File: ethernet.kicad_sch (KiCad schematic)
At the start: 65 parts, among them Q5001 DMG1012T, Q5002 DMG1012T, U1002 AM6231ASGGGAALW, U5001 HR911130A, U5002 RTL8211F-CG, U5003 TPD4E05U06DQA, U5004 TPD4E05U06DQA

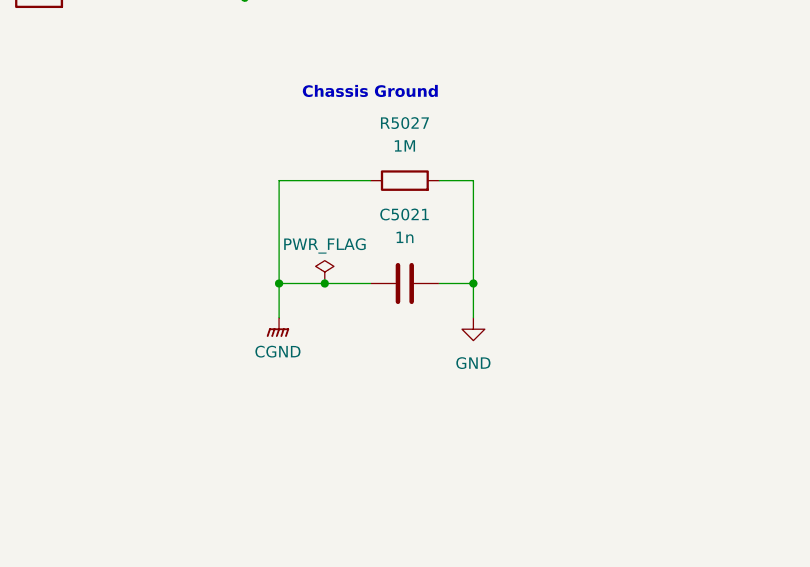
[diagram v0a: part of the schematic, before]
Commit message: All capacitors and crystals added to BOM. 150u cap for USB A changed to tantalum and rerouted
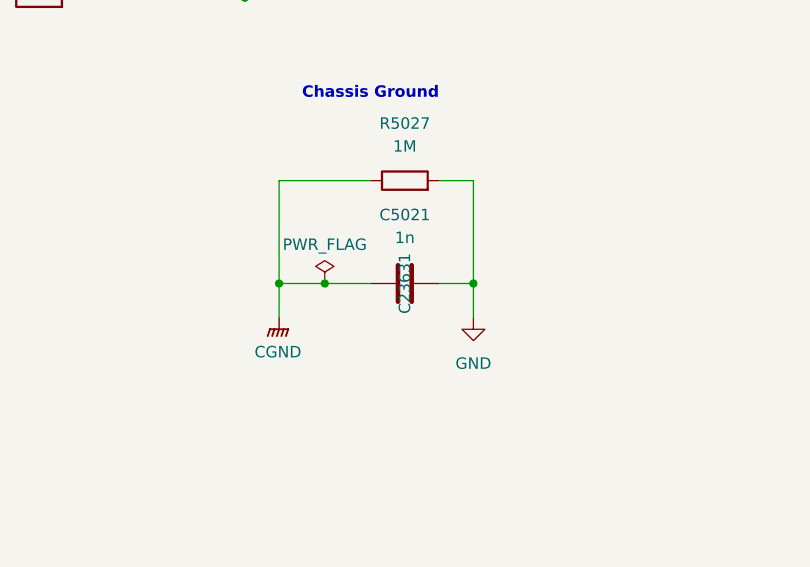
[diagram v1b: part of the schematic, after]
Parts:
- C5021: JLCPCB Part# (none) -> C23631
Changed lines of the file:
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@@
 			)
 		)
-		(property "JLCPCB Part#" ""
+		(property "JLCPCB Part#" " C23631"
 			(at 427.99 307.34 0)
 			(effects

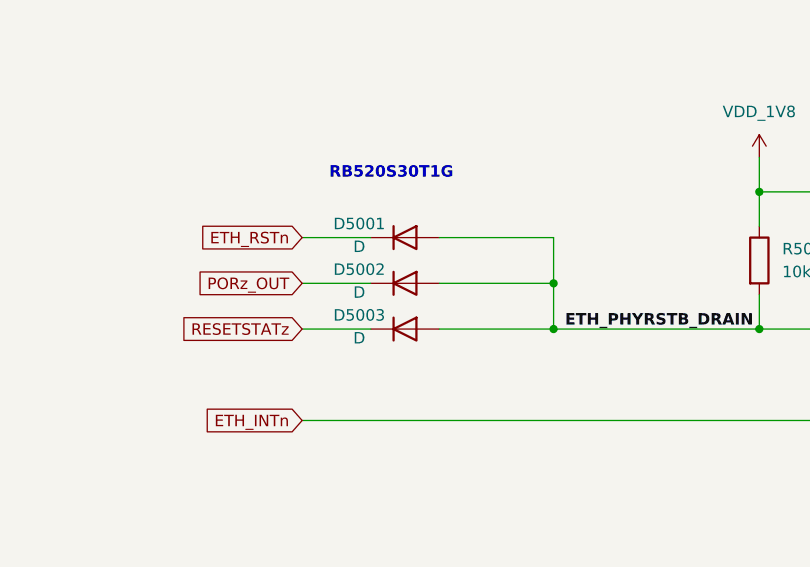
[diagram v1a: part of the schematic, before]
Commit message: Added diode and tvs diode JLC part numbers to BOM. Also fixed tvs diode footprint
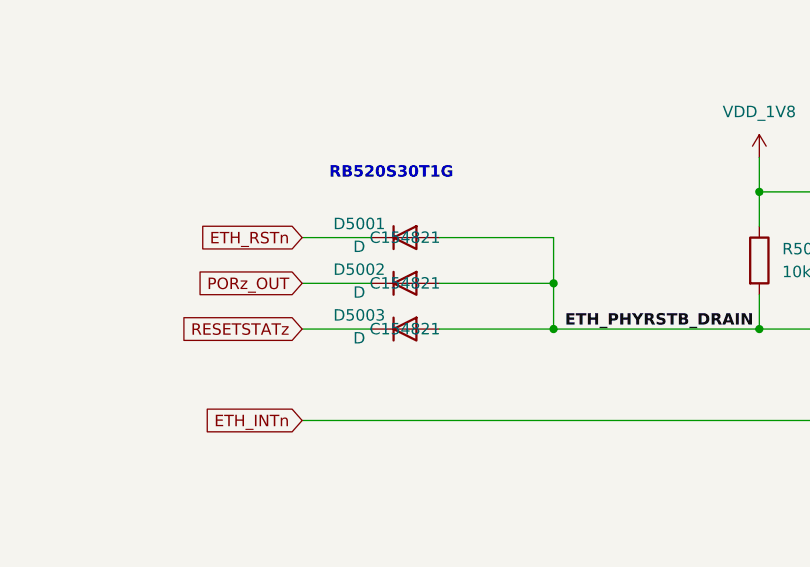
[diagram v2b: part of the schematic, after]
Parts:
- D5001, D5002, D5003: JLCPCB Part# (none) -> C154821
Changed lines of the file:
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@@
 			)
 		)
-		(property "JLCPCB Part#" ""
+		(property "JLCPCB Part#" "C154821"
 			(at 148.59 339.09 0)
 			(effects
@@
 			)
 		)
-		(property "JLCPCB Part#" ""
+		(property "JLCPCB Part#" "C154821"
 			(at 148.59 328.93 0)
 			(effects
@@
 			)
 		)
-		(property "JLCPCB Part#" ""
+		(property "JLCPCB Part#" "C154821"
 			(at 148.59 334.01 0)
 			(effects

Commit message: All JLC part numbers added to BOM except LEDs
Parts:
- FB5001, FB5002: JLCPCB Part# (none) -> C76891
- L5001: JLCPCB Part# (none) -> C391305
- Q5001, Q5002: JLCPCB Part# (none) -> C20512
- R5001, R5002, R5003, R5020, R5022, R5024: JLCPCB Part# (none) -> C105871
- R5004: JLCPCB Part# (none) -> C114759
- R5005, R5006, R5007: JLCPCB Part# (none) -> C106235
- R5008, R5009, R5010, R5011, R5012, R5013, R5014, R5015, R5016, R5017, R5018, R5019, R5021: JLCPCB Part# (none) -> C114765
- R5023: JLCPCB Part# (none) -> C145071
- R5025, R5026: JLCPCB Part# (none) -> C276273
- R5027: JLCPCB Part# (none) -> C108083
- R5028, R5029, R5030, R5031: JLCPCB Part# (none) -> C60490
- U1002: JLCPCB Part# (none) -> C7072556
- U5001: JLCPCB Part# (none) -> C54408
- U5002: JLCPCB Part# (none) -> C187932
- U5003, U5004: JLCPCB Part# (none) -> C138714
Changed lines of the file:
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@@
 			)
 		)
-		(property "JLCPCB Part#" ""
+		(property "JLCPCB Part#" "C76891"
 			(at 214.63 130.81 0)
 			(effects
@@
 			)
 		)
-		(property "JLCPCB Part#" ""
+		(property "JLCPCB Part#" " C276273"
 			(at 387.35 265.43 0)
 			(effects
@@
 			)
 		)
-		(property "JLCPCB Part#" ""
+		(property "JLCPCB Part#" "C114765"
 			(at 240.03 182.88 0)
 			(effects
@@
 			)
 		)
-		(property "JLCPCB Part#" ""
+		(property "JLCPCB Part#" "C114759"
 			(at 520.7 110.49 0)
 			(effects
@@
 			)
 		)
-		(property "JLCPCB Part#" ""
+		(property "JLCPCB Part#" "C114765"
 			(at 240.03 185.42 0)
 			(effects
@@
 			)
 		)
-		(property "JLCPCB Part#" ""
+		(property "JLCPCB Part#" "C108083"
 			(at 427.99 295.91 0)
 			(effects
@@
 			)
 		)
-		(property "JLCPCB Part#" ""
+		(property "JLCPCB Part#" "C105871"
 			(at 387.35 250.19 0)
 			(effects
@@
 			)
 		)
-		(property "JLCPCB Part#" ""
+		(property "JLCPCB Part#" "C145071"
 			(at 351.79 259.08 0)
 			(effects
@@
 			)
 		)
-		(property "JLCPCB Part#" ""
+		(property "JLCPCB Part#" "C114765"
 			(at 144.78 209.55 0)
 			(effects
@@
 			)
 		)
-		(property "JLCPCB Part#" ""
+		(property "JLCPCB Part#" "C105871"
 			(at 387.35 240.03 0)
 			(effects
@@
 			)
 		)
-		(property "JLCPCB Part#" ""
+		(property "JLCPCB Part#" "C60490"
 			(at 231.14 331.47 0)
 			(effects
@@
 			)
 		)
-		(property "JLCPCB Part#" ""
+		(property "JLCPCB Part#" "C20512"
 			(at 248.92 336.55 0)
 			(effects
@@
 			)
 		)
-		(property "JLCPCB Part#" ""
+		(property "JLCPCB Part#" "C138714"
 			(at 422.91 238.76 0)
 			(effects
@@
 			)
 		)
-		(property "JLCPCB Part#" ""
+		(property "JLCPCB Part#" "C114765"
 			(at 144.78 207.01 0)
 			(effects
@@
 			)
 		)
-		(property "JLCPCB Part#" ""
+		(property "JLCPCB Part#" "C105871"
 			(at 364.49 259.08 0)
 			(effects
@@
 			)
 		)
-		(property "JLCPCB Part#" ""
+		(property "JLCPCB Part#" "C114765"
 			(at 240.03 194.31 0)
 			(effects
@@
 			)
 		)
-		(property "JLCPCB Part#" ""
+		(property "JLCPCB Part#" "C114765"
 			(at 240.03 187.96 0)
 			(effects
@@
 			)
 		)
-		(property "JLCPCB Part#" ""
+		(property "JLCPCB Part#" "C60490"
 			(at 217.17 331.47 0)
 			(effects
@@
 			)
 		)
-		(property "JLCPCB Part#" ""
+		(property "JLCPCB Part#" "C106235"
 			(at 468.63 156.21 0)
 			(effects
@@
 			)
 		)
-		(property "JLCPCB Part#" ""
+		(property "JLCPCB Part#" "C106235"
 			(at 458.47 156.21 0)
 			(effects
@@
 			)
 		)
-		(property "JLCPCB Part#" ""
+		(property "JLCPCB Part#" "C7072556"
 			(at 80.01 218.44 0)
 			(effects
@@
 			)
 		)
-		(property "JLCPCB Part#" ""
+		(property "JLCPCB Part#" " C276273"
 			(at 387.35 275.59 0)
 			(effects
@@
 			)
 		)
-		(property "JLCPCB Part#" ""
+		(property "JLCPCB Part#" "C138714"
 			(at 464.82 238.76 0)
 			(effects
@@
 			)
 		)
-		(property "JLCPCB Part#" ""
+		(property "JLCPCB Part#" "C114765"
 			(at 144.78 217.17 0)
 			(effects
@@
 			)
 		)
-		(property "JLCPCB Part#" ""
+		(property "JLCPCB Part#" "C187932"
 			(at 302.26 217.17 0)
 			(effects
@@
 			)
 		)
-		(property "JLCPCB Part#" ""
+		(property "JLCPCB Part#" "C20512"
 			(at 204.47 336.55 0)
 			(effects
@@
 			)
 		)
-		(property "JLCPCB Part#" ""
+		(property "JLCPCB Part#" "C60490"
 			(at 187.96 331.47 0)
 			(effects
@@
 			)
 		)
-		(property "JLCPCB Part#" ""
+		(property "JLCPCB Part#" "C391305"
 			(at 354.33 157.48 0)
 			(effects
@@
 			)
 		)
-		(property "JLCPCB Part#" ""
+		(property "JLCPCB Part#" "C60490"
 			(at 267.97 331.47 0)
 			(effects
@@
 			)
 		)
-		(property "JLCPCB Part#" ""
+		(property "JLCPCB Part#" "C105871"
 			(at 468.63 109.22 0)
 			(effects
@@
 			)
 		)
-		(property "JLCPCB Part#" ""
+		(property "JLCPCB Part#" "C114765"
 			(at 240.03 190.5 0)
 			(effects
@@
 			)
 		)
-		(property "JLCPCB Part#" ""
+		(property "JLCPCB Part#" "C105871"
 			(at 458.47 109.22 0)
 			(effects
@@
 			)
 		)
-		(property "JLCPCB Part#" ""
+		(property "JLCPCB Part#" "C76891"
 			(at 387.35 95.25 0)
 			(effects
@@
 			)
 		)
-		(property "JLCPCB Part#" ""
+		(property "JLCPCB Part#" "C114765"
 			(at 144.78 201.93 0)
 			(effects
@@
 			)
 		)
-		(property "JLCPCB Part#" ""
+		(property "JLCPCB Part#" "C54408"
 			(at 508 212.09 0)
 			(effects
@@
 			)
 		)
-		(property "JLCPCB Part#" ""
+		(property "JLCPCB Part#" "C114765"
 			(at 144.78 213.36 0)
 			(effects
@@
 			)
 		)
-		(property "JLCPCB Part#" ""
+		(property "JLCPCB Part#" "C114765"
 			(at 247.65 248.92 0)
 			(effects
@@
 			)
 		)
-		(property "JLCPCB Part#" ""
+		(property "JLCPCB Part#" "C114765"
 			(at 144.78 204.47 0)
 			(effects
@@
 			)
 		)
-		(property "JLCPCB Part#" ""
+		(property "JLCPCB Part#" "C114765"
 			(at 240.03 198.12 0)
 			(effects
@@
 			)
 		)
-		(property "JLCPCB Part#" ""
+		(property "JLCPCB Part#" "C106235"
 			(at 478.79 156.21 0)
 			(effects
@@
 			)
 		)
-		(property "JLCPCB Part#" ""
+		(property "JLCPCB Part#" "C105871"
 			(at 478.79 109.22 0)
 			(effects

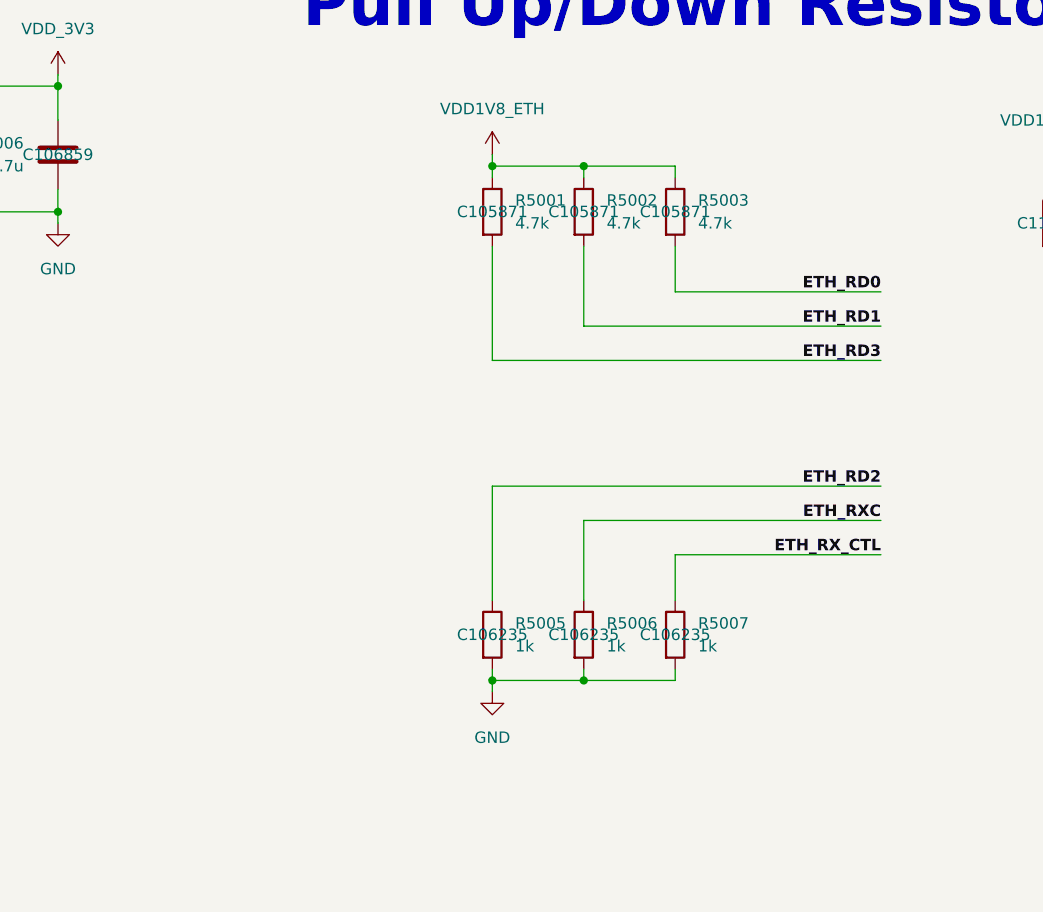
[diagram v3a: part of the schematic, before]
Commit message: Changed ethernet phy strap options and added DNP options for debugging
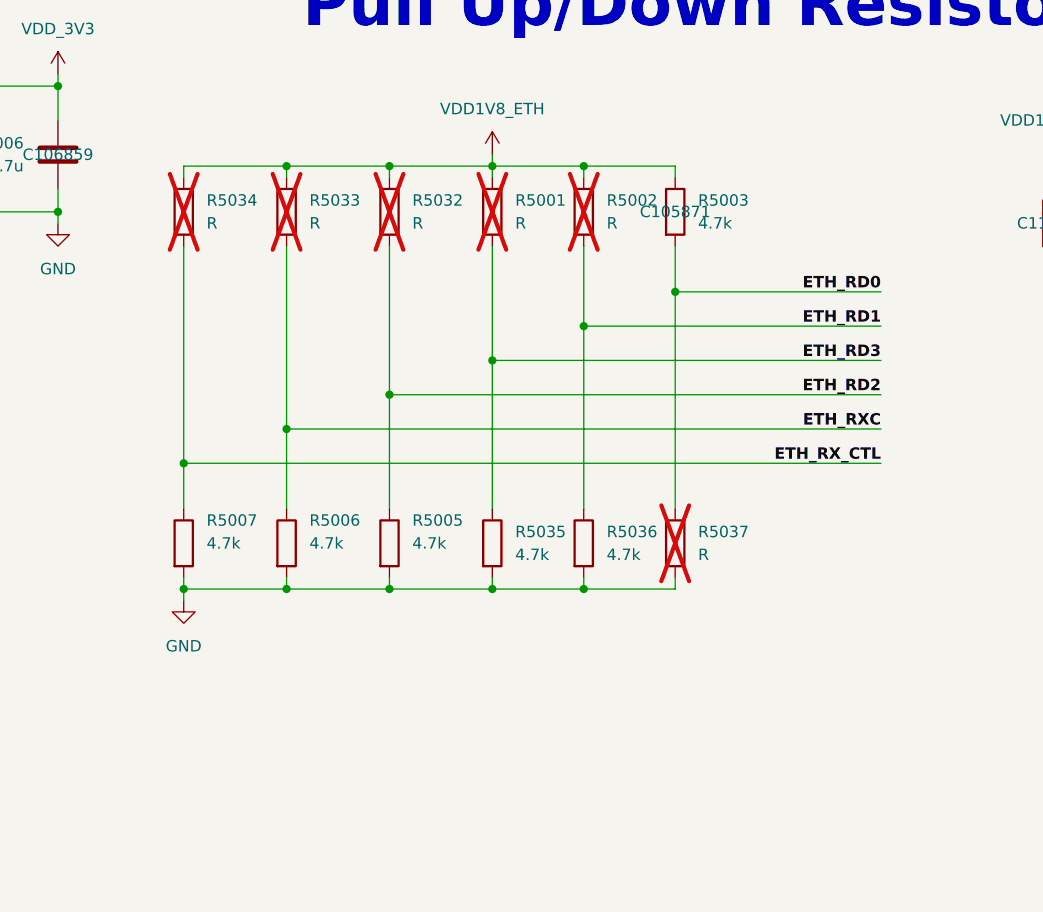
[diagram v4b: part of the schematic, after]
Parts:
- added R5032, R5033, R5034, R5037: R, Resistor_SMD:R_0402_1005Metric, symbol Device:R
- added R5035, R5036: 4.7k, Resistor_SMD:R_0402_1005Metric, symbol Device:R
- R5001, R5002: value 4.7k -> R; JLCPCB Part# C105871 -> (none); now not fitted
- R5005, R5006, R5007: value 1k -> 4.7k; JLCPCB Part# C106235 -> (none)
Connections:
- net ETH_RD0: now also R5037.1
- net ETH_RD1: now also R5036.1
- net ETH_RD2: now also R5032.2
- net ETH_RD3: now also R5035.1
- net ETH_RXC: now also R5033.2
- net ETH_RX_CTL: now also R5034.2
- net GND: now also R5035.2, R5036.2, R5037.2
- net VDD1V8_ETH: now also R5032.1, R5033.1, R5034.1
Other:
- moved on the sheet: R5005, R5006, R5007

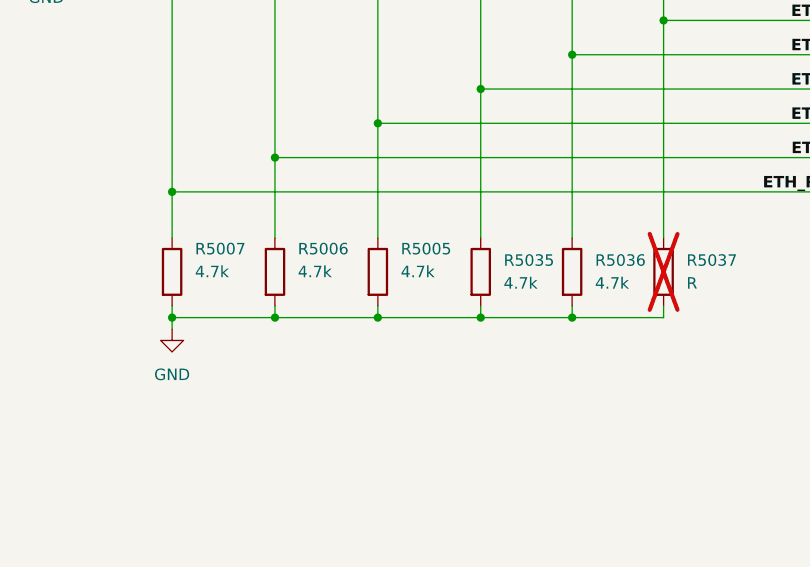
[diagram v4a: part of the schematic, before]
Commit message: Small DDR4 cleanup
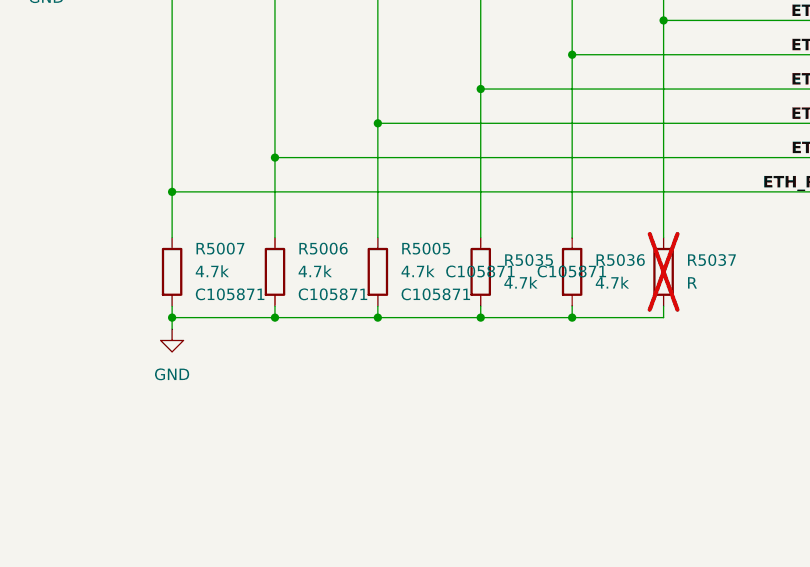
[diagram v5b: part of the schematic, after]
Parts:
- R5005, R5006, R5007, R5035, R5036: JLCPCB Part# (none) -> C105871
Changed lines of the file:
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@@
 			)
 		)
+		(property "JLCPCB Part#" "C105871"
+			(at 458.47 146.05 0)
+			(effects
+				(font
+					(size 1.27 1.27)
+				)
+			)
+		)
 		(pin "1"
 		)
@@
 			)
 		)
-		(property "JLCPCB Part#" ""
+		(property "JLCPCB Part#" "C105871"
 			(at 438.15 148.5899 0)
 			(effects
@@
 			)
 		)
-		(property "JLCPCB Part#" ""
+		(property "JLCPCB Part#" "C105871"
 			(at 449.58 148.5899 0)
 			(effects
@@
 			)
 		)
+		(property "JLCPCB Part#" "C105871"
+			(at 468.63 146.05 0)
+			(effects
+				(font
+					(size 1.27 1.27)
+				)
+			)
+		)
 		(pin "1"
 		)
@@
 			)
 		)
-		(property "JLCPCB Part#" ""
+		(property "JLCPCB Part#" "C105871"
 			(at 426.72 148.5899 0)
 			(effects

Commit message: Fixed Ethernet schematic and strapping. Also fixed some decoupling routing
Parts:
- removed C5011: 4.7u, Capacitor_SMD:C_0402_1005Metric, symbol Device:C
- removed C5012: 0.1u, Capacitor_SMD:C_0402_1005Metric, symbol Device:C
- removed FB5002: 120R, Resistor_SMD:R_0402_1005Metric, symbol Device:FerriteBead
- removed R5025: 510R, Resistor_SMD:R_0402_1005Metric, symbol Device:R
- added FB5003: 120R, Resistor_SMD:R_0402_1005Metric, symbol Device:FerriteBead
- added R5038: R, Resistor_SMD:R_0402_1005Metric, symbol Device:R
- added R5039: 510R, Resistor_SMD:R_0402_1005Metric, symbol Device:R
- C5005: value 0.1u -> 1u; JLCPCB Part# C60474 -> (none)
- C5006: value 4.7u -> 1u; JLCPCB Part# C106859 -> (none)
- R5021: value 22R -> 0R; JLCPCB Part# C114765 -> (none)
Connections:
- net ETH_LED_GREEN_K is gone; now on net GND: U5001.12 (LED_GREEN_K)
- net ETH_CFG_EXIT/LED0: now also R5020.2; no longer R5020.1
- net ETH_CFG_LDO0/LED1: now also R5039.1
- net GND: now also R5020.1
- net VDD1V0_ETH: now also C5005.1, C5006.1
- net VDD1V8_ETH: now also R5038.2
- net VDD3V3_ETH: no longer C5001.1, C5002.1, C5003.1, C5004.1, FB5001.1, U5002.11 (AVDD33), U5002.40 (AVDD33)
- net VDD_1V8: now also R5038.1
- net VDD_3V3: now also FB5003.1; no longer C5005.1, C5006.1, C5016.1, C5017.1, R5020.2, R5022.2, U5001.11 (LED_GREEN_A), U5001.14 (LED_YELLOW_A), U5002.29 (DVDD33)
- new net DVDD3V3_ETH: C5016.1, C5017.1, FB5003.2, R5022.2, U5001.14 (LED_YELLOW_A), U5002.29 (DVDD33)
- new net ETH_LED_GREEN_A: R5039.2, U5001.11 (LED_GREEN_A)
- new net VDDA3V3_ETH: C5001.1, C5002.1, C5003.1, C5004.1, FB5001.1, U5002.11 (AVDD33), U5002.40 (AVDD33)
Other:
- note added: "X5R Ceramic"
- moved on the sheet: C5001, C5002, C5004, C5007, C5008, C5009, C5013, C5014, C5015, C5021, R5020, R5022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
